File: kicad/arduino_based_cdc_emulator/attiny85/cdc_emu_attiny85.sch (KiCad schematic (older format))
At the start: 9 parts, among them IC1 ATTINY85-S, P1 CONN_5, U1 78L05

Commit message: board for attiny version vwcdavr smd
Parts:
- removed U1: 78L05, symbol 78L05
- added C3: 1u/6.3V, Capacitors_SMD:C_0805_HandSoldering, symbol CP
- added P2: CONN_01X03, Pin_Headers:Pin_Header_Straight_1x03, symbol CONN_01X03
- added U1: AP1117D50, TO_SOT_Packages_SMD:SOT-223, symbol AP1117D50
- added U2: LM78L05ACZ, Housings_SOT-23_SOT-143_TSOT-6:SOT-23, symbol LM78L05ACZ
- C1, C2: footprint (none) -> Capacitors_SMD:C_0805_HandSoldering; symbol C -> C-RESCUE-cdc_emu_attiny85
- IC1: symbol ATTINY85-S -> ATTINY85-S-RESCUE-cdc_emu_attiny85
- P1: value CONN_5 -> CONN_01X05; footprint (none) -> Pin_Headers:Pin_Header_Straight_1x05; symbol CONN_5 -> CONN_01X05
- R1, R2, R3, R4: footprint (none) -> Resistors_SMD:R_0805_HandSoldering; symbol R -> R-RESCUE-cdc_emu_attiny85
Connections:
- net labels added: MOSI, RST, TX
- wire segments 27 -> 41
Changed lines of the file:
@@
-EESchema Schematic File Version 2  date Tue 04 Mar 2014 02:18:31 PM CET
+EESchema Schematic File Version 2
+LIBS:cdc_emu_attiny85-rescue
 LIBS:power
 LIBS:device
@@
 LIBS:memory
 LIBS:xilinx
-LIBS:special
 LIBS:microcontrollers
 LIBS:dsp
@@
 LIBS:valves
 LIBS:cdc_emu_attiny85-cache
-EELAYER 25  0
+EELAYER 25 0
 EELAYER END
-$Descr A4 11700 8267
+$Descr A4 11693 8268
 encoding utf-8
 Sheet 1 1
@@
 	3950 3500 3500 3500
 Wire Wire Line
-	3950 3800 3850 3800
-Wire Wire Line
-	3850 3800 3850 3050
+	3500 3800 3950 3800
+Wire Wire Line
+	3850 3050 3850 3800
 Wire Wire Line
 	7400 3300 7300 3300
@@
 F 0 "#PWR01" H 8950 4350 20  0001 C CNN
 F 1 "+12V" H 8950 4500 30  0000 C CNN
+F 2 "" H 8950 4400 60  0001 C CNN
+F 3 "" H 8950 4400 60  0001 C CNN
 	1    8950 4400
 	1    0    0    -1
 $EndComp
 $Comp
-L GND #PWR02
+L GND-RESCUE-cdc_emu_attiny85 #PWR02
 U 1 1 531578E1
 P 9050 4550
 F 0 "#PWR02" H 9050 4550 30  0001 C CNN
 F 1 "GND" H 9050 4480 30  0001 C CNN
+F 2 "" H 9050 4550 60  0001 C CNN
+F 3 "" H 9050 4550 60  0001 C CNN
 	1    9050 4550
 	1    0    0    -1
@@
 DataIn
 $Comp
-L CONN_5 P1
+L CONN_01X05 P1
 U 1 1 531578B2
-P 9650 4250
-F 0 "P1" V 9600 4250 50  0000 C CNN
-F 1 "CONN_5" V 9700 4250 50  0000 C CNN
-	1    9650 4250
+P 9450 4250
+F 0 "P1" V 9400 4250 50  0000 C CNN
+F 1 "CONN_01X05" V 9500 4250 50  0000 C CNN
+F 2 "Pin_Headers:Pin_Header_Straight_1x05" H 9450 4250 60  0001 C CNN
+F 3 "" H 9450 4250 60  0001 C CNN
+	1    9450 4250
 	1    0    0    -1
 $EndComp
@@
 F 0 "#PWR03" H 6650 5350 20  0001 C CNN
 F 1 "+12V" H 6650 5500 30  0000 C CNN
+F 2 "" H 6650 5400 60  0001 C CNN
+F 3 "" H 6650 5400 60  0001 C CNN
 	1    6650 5400
 	1    0    0    -1
@@
 F 0 "#PWR04" H 7750 5490 20  0001 C CNN
 F 1 "+5V" H 7750 5490 30  0000 C CNN
+F 2 "" H 7750 5400 60  0001 C CNN
+F 3 "" H 7750 5400 60  0001 C CNN
 	1    7750 5400
 	1    0    0    -1
 $EndComp
 $Comp
-L GND #PWR05
+L GND-RESCUE-cdc_emu_attiny85 #PWR05
 U 1 1 53148A75
 P 7750 6100
 F 0 "#PWR05" H 7750 6100 30  0001 C CNN
 F 1 "GND" H 7750 6030 30  0001 C CNN
+F 2 "" H 7750 6100 60  0001 C CNN
+F 3 "" H 7750 6100 60  0001 C CNN
 	1    7750 6100
 	1    0    0    -1
 $EndComp
 $Comp
-L GND #PWR06
+L GND-RESCUE-cdc_emu_attiny85 #PWR06
 U 1 1 53148A72
 P 7200 6100
 F 0 "#PWR06" H 7200 6100 30  0001 C CNN
 F 1 "GND" H 7200 6030 30  0001 C CNN
+F 2 "" H 7200 6100 60  0001 C CNN
+F 3 "" H 7200 6100 60  0001 C CNN
 	1    7200 6100
 	1    0    0    -1
 $EndComp
 $Comp
-L GND #PWR07
+L GND-RESCUE-cdc_emu_attiny85 #PWR07
 U 1 1 53148A70
 P 6650 6100
 F 0 "#PWR07" H 6650 6100 30  0001 C CNN
 F 1 "GND" H 6650 6030 30  0001 C CNN
+F 2 "" H 6650 6100 60  0001 C CNN
+F 3 "" H 6650 6100 60  0001 C CNN
 	1    6650 6100
 	1    0    0    -1
 $EndComp
 $Comp
-L C C2
+L C-RESCUE-cdc_emu_attiny85 C2
 U 1 1 53148A27
 P 7750 5800
 F 0 "C2" H 7800 5900 50  0000 L CNN
 F 1 "100n" H 7800 5700 50  0000 L CNN
+F 2 "Capacitors_SMD:C_0805_HandSoldering" H 7750 5800 60  0001 C CNN
+F 3 "" H 7750 5800 60  0001 C CNN
 	1    7750 5800
 	1    0    0    -1
 $EndComp
 $Comp
-L C C1
+L C-RESCUE-cdc_emu_attiny85 C1
 U 1 1 53148A21
 P 6650 5800
 F 0 "C1" H 6700 5900 50  0000 L CNN
 F 1 "100n" H 6700 5700 50  0000 L CNN
+F 2 "Capacitors_SMD:C_0805_HandSoldering" H 6650 5800 60  0001 C CNN
+F 3 "" H 6650 5800 60  0001 C CNN
 	1    6650 5800
 	1    0    0    -1
 $EndComp
 $Comp
-L 78L05 U1
-U 1 1 53148A1A
-P 7200 5550
-F 0 "U1" H 7350 5354 60  0000 C CNN
-F 1 "78L05" H 7200 5750 60  0000 C CNN
-	1    7200 5550
-	1    0    0    -1
-$EndComp
-$Comp
-L GND #PWR08
+L GND-RESCUE-cdc_emu_attiny85 #PWR08
 U 1 1 53148A0A
 P 7300 3900
 F 0 "#PWR08" H 7300 3900 30  0001 C CNN
 F 1 "GND" H 7300 3830 30  0001 C CNN
+F 2 "" H 7300 3900 60  0001 C CNN
+F 3 "" H 7300 3900 60  0001 C CNN
 	1    7300 3900
 	1    0    0    -1
@@
 F 0 "#PWR09" H 7400 3040 20  0001 C CNN
 F 1 "+5V" H 7400 3040 30  0000 C CNN
+F 2 "" H 7400 2950 60  0001 C CNN
+F 3 "" H 7400 2950 60  0001 C CNN
 	1    7400 2950
 	1    0    0    -1
 $EndComp
 $Comp
-L R R3
+L R-RESCUE-cdc_emu_attiny85 R3
 U 1 1 531489A2
 P 4200 3700
-F 0 "R3" V 4280 3700 50  0000 C CNN
+F 0 "R3" V 4150 3900 50  0000 C CNN
 F 1 "3k3" V 4200 3700 50  0000 C CNN
+F 2 "Resistors_SMD:R_0805_HandSoldering" H 4200 3700 60  0001 C CNN
+F 3 "" H 4200 3700 60  0001 C CNN
 	1    4200 3700
 	0    -1   -1   0
 $EndComp
 $Comp
-L R R2
+L R-RESCUE-cdc_emu_attiny85 R2
 U 1 1 5314899E
 P 4200 3500
-F 0 "R2" V 4280 3500 50  0000 C CNN
+F 0 "R2" V 4150 3700 50  0000 C CNN
 F 1 "3k3" V 4200 3500 50  0000 C CNN
+F 2 "Resistors_SMD:R_0805_HandSoldering" H 4200 3500 60  0001 C CNN
+F 3 "" H 4200 3500 60  0001 C CNN
 	1    4200 3500
 	0    -1   -1   0
 $EndComp
 $Comp
-L R R1
+L R-RESCUE-cdc_emu_attiny85 R1
 U 1 1 53148999
 P 4200 3400
-F 0 "R1" V 4280 3400 50  0000 C CNN
+F 0 "R1" V 4150 3600 50  0000 C CNN
 F 1 "3k3" V 4200 3400 50  0000 C CNN
+F 2 "Resistors_SMD:R_0805_HandSoldering" H 4200 3400 60  0001 C CNN
+F 3 "" H 4200 3400 60  0001 C CNN
 	1    4200 3400
 	0    -1   -1   0
 $EndComp
 $Comp
-L R R4
+L R-RESCUE-cdc_emu_attiny85 R4
 U 1 1 53148995
 P 4200 3800
-F 0 "R4" V 4280 3800 50  0000 C CNN
+F 0 "R4" V 4100 4000 50  0000 C CNN
 F 1 "10k" V 4200 3800 50  0000 C CNN
+F 2 "Resistors_SMD:R_0805_HandSoldering" H 4200 3800 60  0001 C CNN
+F 3 "" H 4200 3800 60  0001 C CNN
 	1    4200 3800
 	0    -1   -1   0
 $EndComp
 $Comp
-L ATTINY85-S IC1
+L ATTINY85-S-RESCUE-cdc_emu_attiny85 IC1
 U 1 1 53148881
 P 4800 3200
@@
 F 1 "ATTINY85-S" H 6800 2450 60  0000 C CNN
 F 2 "DIP8" H 4900 2450 60  0001 C CNN
+F 3 "" H 4800 3200 60  0001 C CNN
 	1    4800 3200
 	1    0    0    -1
 $EndComp
+$Comp
+L CP C3
+U 1 1 560DAE88
+P 4550 4150
+F 0 "C3" H 4575 4250 50  0000 L CNN
+F 1 "1u/6.3V" H 4575 4050 50  0000 L CNN
+F 2 "Capacitors_SMD:C_0805_HandSoldering" H 4588 4000 30  0000 C CNN
+F 3 "" H 4550 4150 60  0000 C CNN
+	1    4550 4150
+	1    0    0    -1
+$EndComp
+Wire Wire Line
+	4550 4000 4550 3800
+Connection ~ 4550 3800
+Wire Wire Line
+	4550 4300 4550 4400
+$Comp
+L GND-RESCUE-cdc_emu_attiny85 #PWR010
+U 1 1 560DAF73
+P 4550 4400
+F 0 "#PWR010" H 4550 4400 30  0001 C CNN
+F 1 "GND" H 4550 4330 30  0001 C CNN
+F 2 "" H 4550 4400 60  0001 C CNN
+F 3 "" H 4550 4400 60  0001 C CNN
+	1    4550 4400
+	1    0    0    -1
+$EndComp
+Wire Wire Line
+	3500 3600 4600 3600
+Wire Wire Line
+	9250 3450 8450 3450
+Text Label 8450 3450 0    60   ~ 0
+TX
+Text Label 3500 3600 0    60   ~ 0
+TX
+Wire Wire Line
+	3500 3300 4600 3300
+Text Label 3500 3300 0    60   ~ 0
+MOSI
+Connection ~ 3850 3800
+Text Label 3500 3800 0    60   ~ 0
+RST
+Text Label 8450 3350 0    60   ~ 0
+MOSI
+Text Label 8450 3550 0    60   ~ 0
+RST
+Wire Wire Line
+	8450 3550 9250 3550
+Wire Wire Line
+	8450 3350 9250 3350
+$Comp
+L CONN_01X03 P2
+U 1 1 5628FA6F
+P 9450 3450
+F 0 "P2" V 9400 3450 50  0000 C CNN
+F 1 "CONN_01X03" V 9500 3450 50  0000 C CNN
+F 2 "Pin_Headers:Pin_Header_Straight_1x03" H 9450 3450 60  0001 C CNN
+F 3 "" H 9450 3450 60  0001 C CNN
+	1    9450 3450
+	1    0    0    -1
+$EndComp
+$Comp
+L AP1117D50 U1
+U 1 1 562904CD
+P 7200 4900
+F 0 "U1" H 7300 4650 50  0000 C CNN
+F 1 "AP1117D50" H 7200 5150 50  0000 C CNN
+F 2 "TO_SOT_Packages_SMD:SOT-223" H 7200 4900 60  0000 C CNN
+F 3 "" H 7200 4900 60  0000 C CNN
+	1    7200 4900
+	1    0    0    -1
+$EndComp
+Wire Wire Line
+	7200 5200 7450 5200
+Wire Wire Line
+	7450 5200 7450 5900
+Wire Wire Line
+	7450 5900 7200 5900
+Connection ~ 7200 5900
+Wire Wire Line
+	6750 4900 6900 4900
+Wire Wire Line
+	6750 4900 6750 5500
+Connection ~ 6750 5500
+Wire Wire Line
+	7650 5500 7650 4900
+Wire Wire Line
+	7650 4900 7500 4900
+Connection ~ 7650 5500
+$Comp
+L LM78L05ACZ U2
+U 1 1 56290767
+P 7200 5550
+F 0 "U2" H 7000 5750 40  0000 C CNN
+F 1 "LM78L05ACZ" H 7200 5750 40  0000 L CNN
+F 2 "Housings_SOT-23_SOT-143_TSOT-6:SOT-23" H 7200 5650 30  0000 C CIN
+F 3 "" H 7200 5550 60  0000 C CNN
+	1    7200 5550
+	1    0    0    -1
+$EndComp

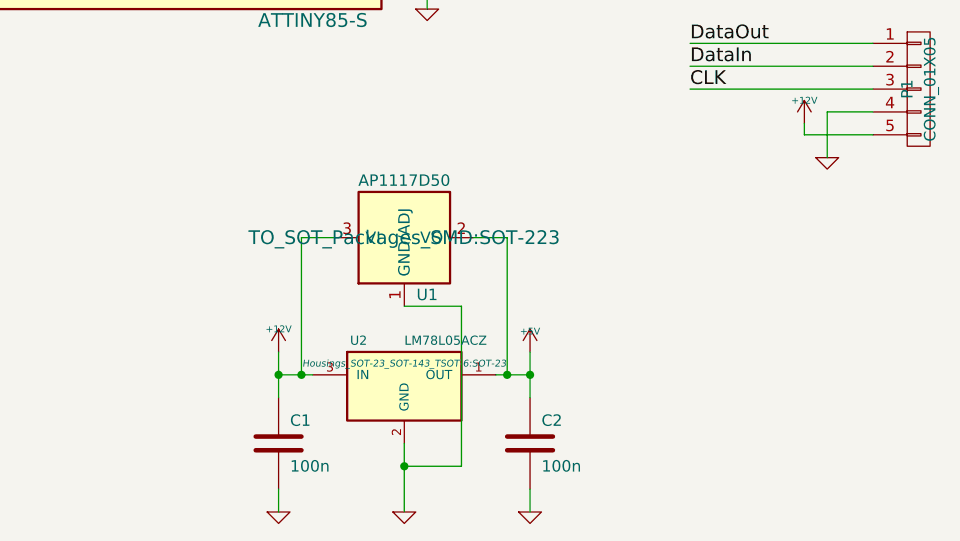
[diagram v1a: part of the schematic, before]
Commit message: fix 78L05 pinout, 5V connection from U1
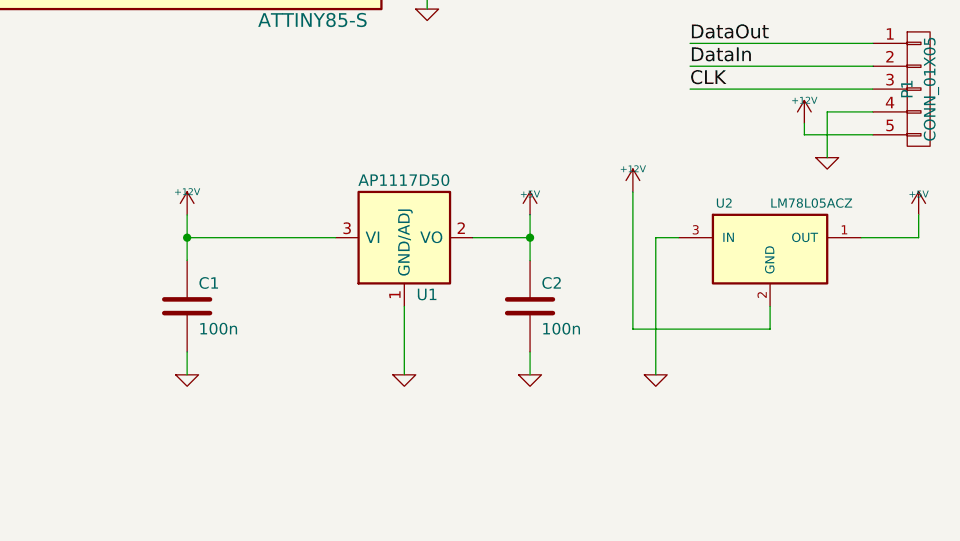
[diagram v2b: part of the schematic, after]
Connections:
- net +12V: now also U2.2 (GND); no longer U2.3 (IN)
- net GND: now also U2.3 (IN); no longer U2.2 (GND)
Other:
- moved on the sheet: C1, C2, U2
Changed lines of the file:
@@
 Comment4 ""
 $EndDescr
-Wire Wire Line
-	8950 4400 8950 4450
-Wire Wire Line
-	8950 4450 9250 4450
-Wire Wire Line
-	4450 3500 4600 3500
-Wire Wire Line
-	4450 3800 4600 3800
-Wire Wire Line
-	7400 3050 3850 3050
-Wire Wire Line
-	9250 4250 8450 4250
-Wire Wire Line
-	9250 4050 8450 4050
-Wire Wire Line
-	7750 6000 7750 6100
-Wire Wire Line
-	6650 6000 6650 6100
-Wire Wire Line
-	6650 5500 6800 5500
-Wire Wire Line
-	7750 5400 7750 5600
-Connection ~ 7400 3050
-Wire Wire Line
-	7400 2950 7400 3300
-Wire Wire Line
-	3950 3700 3500 3700
-Wire Wire Line
-	3500 3400 3950 3400
-Wire Wire Line
-	3950 3500 3500 3500
-Wire Wire Line
-	3500 3800 3950 3800
-Wire Wire Line
-	3850 3050 3850 3800
-Wire Wire Line
-	7400 3300 7300 3300
-Wire Wire Line
-	7600 5500 7750 5500
-Connection ~ 7750 5500
-Wire Wire Line
-	6650 5400 6650 5600
-Connection ~ 6650 5500
-Wire Wire Line
-	7200 5800 7200 6100
-Wire Wire Line
-	9250 4150 8450 4150
-Wire Wire Line
-	4450 3400 4600 3400
-Wire Wire Line
-	4450 3700 4600 3700
-Wire Wire Line
-	7300 3800 7300 3900
-Wire Wire Line
-	9250 4350 9050 4350
-Wire Wire Line
-	9050 4350 9050 4550
 $Comp
 L +12V #PWR01
@@
 L +12V #PWR03
 U 1 1 53148C3B
-P 6650 5400
-F 0 "#PWR03" H 6650 5350 20  0001 C CNN
-F 1 "+12V" H 6650 5500 30  0000 C CNN
-F 2 "" H 6650 5400 60  0001 C CNN
-F 3 "" H 6650 5400 60  0001 C CNN
-	1    6650 5400
+P 6250 4800
+F 0 "#PWR03" H 6250 4750 20  0001 C CNN
+F 1 "+12V" H 6250 4900 30  0000 C CNN
+F 2 "" H 6250 4800 60  0001 C CNN
+F 3 "" H 6250 4800 60  0001 C CNN
+	1    6250 4800
 	1    0    0    -1
 $EndComp
@@
 L +5V #PWR04
 U 1 1 53148C2D
-P 7750 5400
-F 0 "#PWR04" H 7750 5490 20  0001 C CNN
-F 1 "+5V" H 7750 5490 30  0000 C CNN
-F 2 "" H 7750 5400 60  0001 C CNN
-F 3 "" H 7750 5400 60  0001 C CNN
-	1    7750 5400
+P 7750 4800
+F 0 "#PWR04" H 7750 4890 20  0001 C CNN
+F 1 "+5V" H 7750 4890 30  0000 C CNN
+F 2 "" H 7750 4800 60  0001 C CNN
+F 3 "" H 7750 4800 60  0001 C CNN
+	1    7750 4800
 	1    0    0    -1
 $EndComp
@@
 L GND-RESCUE-cdc_emu_attiny85 #PWR05
 U 1 1 53148A75
-P 7750 6100
-F 0 "#PWR05" H 7750 6100 30  0001 C CNN
-F 1 "GND" H 7750 6030 30  0001 C CNN
-F 2 "" H 7750 6100 60  0001 C CNN
-F 3 "" H 7750 6100 60  0001 C CNN
-	1    7750 6100
+P 7750 5500
+F 0 "#PWR05" H 7750 5500 30  0001 C CNN
+F 1 "GND" H 7750 5430 30  0001 C CNN
+F 2 "" H 7750 5500 60  0001 C CNN
+F 3 "" H 7750 5500 60  0001 C CNN
+	1    7750 5500
 	1    0    0    -1
 $EndComp
@@
 L GND-RESCUE-cdc_emu_attiny85 #PWR06
 U 1 1 53148A72
-P 7200 6100
-F 0 "#PWR06" H 7200 6100 30  0001 C CNN
-F 1 "GND" H 7200 6030 30  0001 C CNN
-F 2 "" H 7200 6100 60  0001 C CNN
-F 3 "" H 7200 6100 60  0001 C CNN
-	1    7200 6100
+P 7200 5500
+F 0 "#PWR06" H 7200 5500 30  0001 C CNN
+F 1 "GND" H 7200 5430 30  0001 C CNN
+F 2 "" H 7200 5500 60  0001 C CNN
+F 3 "" H 7200 5500 60  0001 C CNN
+	1    7200 5500
 	1    0    0    -1
 $EndComp
@@
 L GND-RESCUE-cdc_emu_attiny85 #PWR07
 U 1 1 53148A70
-P 6650 6100
-F 0 "#PWR07" H 6650 6100 30  0001 C CNN
-F 1 "GND" H 6650 6030 30  0001 C CNN
-F 2 "" H 6650 6100 60  0001 C CNN
-F 3 "" H 6650 6100 60  0001 C CNN
-	1    6650 6100
+P 6250 5500
+F 0 "#PWR07" H 6250 5500 30  0001 C CNN
+F 1 "GND" H 6250 5430 30  0001 C CNN
+F 2 "" H 6250 5500 60  0001 C CNN
+F 3 "" H 6250 5500 60  0001 C CNN
+	1    6250 5500
 	1    0    0    -1
 $EndComp
@@
 L C-RESCUE-cdc_emu_attiny85 C2
 U 1 1 53148A27
-P 7750 5800
-F 0 "C2" H 7800 5900 50  0000 L CNN
-F 1 "100n" H 7800 5700 50  0000 L CNN
-F 2 "Capacitors_SMD:C_0805_HandSoldering" H 7750 5800 60  0001 C CNN
-F 3 "" H 7750 5800 60  0001 C CNN
-	1    7750 5800
+P 7750 5200
+F 0 "C2" H 7800 5300 50  0000 L CNN
+F 1 "100n" H 7800 5100 50  0000 L CNN
+F 2 "Capacitors_SMD:C_0805_HandSoldering" H 7750 5200 60  0001 C CNN
+F 3 "" H 7750 5200 60  0001 C CNN
+	1    7750 5200
 	1    0    0    -1
 $EndComp
@@
 L C-RESCUE-cdc_emu_attiny85 C1
 U 1 1 53148A21
-P 6650 5800
-F 0 "C1" H 6700 5900 50  0000 L CNN
-F 1 "100n" H 6700 5700 50  0000 L CNN
-F 2 "Capacitors_SMD:C_0805_HandSoldering" H 6650 5800 60  0001 C CNN
-F 3 "" H 6650 5800 60  0001 C CNN
-	1    6650 5800
+P 6250 5200
+F 0 "C1" H 6300 5300 50  0000 L CNN
+F 1 "100n" H 6300 5100 50  0000 L CNN
+F 2 "Capacitors_SMD:C_0805_HandSoldering" H 6250 5200 60  0001 C CNN
+F 3 "" H 6250 5200 60  0001 C CNN
+	1    6250 5200
 	1    0    0    -1
 $EndComp
@@
 	1    0    0    -1
 $EndComp
-Wire Wire Line
-	4550 4000 4550 3800
-Connection ~ 4550 3800
-Wire Wire Line
-	4550 4300 4550 4400
 $Comp
 L GND-RESCUE-cdc_emu_attiny85 #PWR010
@@
 	1    0    0    -1
 $EndComp
-Wire Wire Line
-	3500 3600 4600 3600
-Wire Wire Line
-	9250 3450 8450 3450
 Text Label 8450 3450 0    60   ~ 0
 TX
 Text Label 3500 3600 0    60   ~ 0
 TX
-Wire Wire Line
-	3500 3300 4600 3300
 Text Label 3500 3300 0    60   ~ 0
 MOSI
-Connection ~ 3850 3800
 Text Label 3500 3800 0    60   ~ 0
 RST
@@
 Text Label 8450 3550 0    60   ~ 0
 RST
-Wire Wire Line
-	8450 3550 9250 3550
-Wire Wire Line
-	8450 3350 9250 3350
 $Comp
 L CONN_01X03 P2
@@
 F 0 "U1" H 7300 4650 50  0000 C CNN
 F 1 "AP1117D50" H 7200 5150 50  0000 C CNN
-F 2 "TO_SOT_Packages_SMD:SOT-223" H 7200 4900 60  0000 C CNN
+F 2 "TO_SOT_Packages_SMD:SOT-223" H 7200 4900 60  0001 C CNN
 F 3 "" H 7200 4900 60  0000 C CNN
 	1    7200 4900
 	1    0    0    -1
 $EndComp
-Wire Wire Line
-	7200 5200 7450 5200
-Wire Wire Line
-	7450 5200 7450 5900
-Wire Wire Line
-	7450 5900 7200 5900
-Connection ~ 7200 5900
-Wire Wire Line
-	6750 4900 6900 4900
-Wire Wire Line
-	6750 4900 6750 5500
-Connection ~ 6750 5500
-Wire Wire Line
-	7650 5500 7650 4900
-Wire Wire Line
-	7650 4900 7500 4900
-Connection ~ 7650 5500
 $Comp
 L LM78L05ACZ U2
 U 1 1 56290767
-P 7200 5550
-F 0 "U2" H 7000 5750 40  0000 C CNN
-F 1 "LM78L05ACZ" H 7200 5750 40  0000 L CNN
-F 2 "Housings_SOT-23_SOT-143_TSOT-6:SOT-23" H 7200 5650 30  0000 C CIN
-F 3 "" H 7200 5550 60  0000 C CNN
-	1    7200 5550
-	1    0    0    -1
-$EndComp
+P 8800 4950
+F 0 "U2" H 8600 5150 40  0000 C CNN
+F 1 "LM78L05ACZ" H 8800 5150 40  0000 L CNN
+F 2 "Housings_SOT-23_SOT-143_TSOT-6:SOT-23" H 8800 5050 30  0001 C CIN
+F 3 "" H 8800 4950 60  0000 C CNN
+	1    8800 4950
+	1    0    0    -1
+$EndComp
+Wire Wire Line
+	8950 4400 8950 4450
+Wire Wire Line
+	8950 4450 9250 4450
+Wire Wire Line
+	4450 3500 4600 3500
+Wire Wire Line
+	4450 3800 4600 3800
+Wire Wire Line
+	7400 3050 3850 3050
+Wire Wire Line
+	9250 4250 8450 4250
+Wire Wire Line
+	9250 4050 8450 4050
+Wire Wire Line
+	7750 5400 7750 5500
+Wire Wire Line
+	6250 5400 6250 5500
+Wire Wire Line
+	6250 4900 6900 4900
+Connection ~ 7400 3050
+Wire Wire Line
+	7400 2950 7400 3300
+Wire Wire Line
+	3950 3700 3500 3700
+Wire Wire Line
+	3500 3400 3950 3400
+Wire Wire Line
+	3950 3500 3500 3500
+Wire Wire Line
+	3500 3800 3950 3800
+Wire Wire Line
+	3850 3050 3850 3800
+Wire Wire Line
+	7400 3300 7300 3300
+Wire Wire Line
+	6250 4800 6250 5000
+Connection ~ 6250 4900
+Wire Wire Line
+	9250 4150 8450 4150
+Wire Wire Line
+	4450 3400 4600 3400
+Wire Wire Line
+	4450 3700 4600 3700
+Wire Wire Line
+	7300 3800 7300 3900
+Wire Wire Line
+	9250 4350 9050 4350
+Wire Wire Line
+	9050 4350 9050 4550
+Wire Wire Line
+	4550 4000 4550 3800
+Connection ~ 4550 3800
+Wire Wire Line
+	4550 4300 4550 4400
+Wire Wire Line
+	3500 3600 4600 3600
+Wire Wire Line
+	9250 3450 8450 3450
+Wire Wire Line
+	3500 3300 4600 3300
+Connection ~ 3850 3800
+Wire Wire Line
+	8450 3550 9250 3550
+Wire Wire Line
+	8450 3350 9250 3350
+Wire Wire Line
+	7500 4900 7750 4900
+Wire Wire Line
+	7200 5500 7200 5200
+Wire Wire Line
+	7750 4800 7750 5000
+Connection ~ 7750 4900
+$Comp
+L GND-RESCUE-cdc_emu_attiny85 #PWR?
+U 1 1 56E18351
+P 8300 5500
+F 0 "#PWR?" H 8300 5500 30  0001 C CNN
+F 1 "GND" H 8300 5430 30  0001 C CNN
+F 2 "" H 8300 5500 60  0001 C CNN
+F 3 "" H 8300 5500 60  0001 C CNN
+	1    8300 5500
+	1    0    0    -1
+$EndComp
+Wire Wire Line
+	8300 4900 8300 5500
+$Comp
+L +5V #PWR?
+U 1 1 56E18370
+P 9450 4800
+F 0 "#PWR?" H 9450 4890 20  0001 C CNN
+F 1 "+5V" H 9450 4890 30  0000 C CNN
+F 2 "" H 9450 4800 60  0001 C CNN
+F 3 "" H 9450 4800 60  0001 C CNN
+	1    9450 4800
+	1    0    0    -1
+$EndComp
+Wire Wire Line
+	9200 4900 9450 4900
+Wire Wire Line
+	9450 4900 9450 4800
+$Comp
+L +12V #PWR?
+U 1 1 56E184F4
+P 8200 4700
+F 0 "#PWR?" H 8200 4650 20  0001 C CNN
+F 1 "+12V" H 8200 4800 30  0000 C CNN
+F 2 "" H 8200 4700 60  0001 C CNN
+F 3 "" H 8200 4700 60  0001 C CNN
+	1    8200 4700
+	1    0    0    -1
+$EndComp
+Wire Wire Line
+	8200 4700 8200 5300
+Wire Wire Line
+	8300 4900 8400 4900
+Wire Wire Line
+	8200 5300 8800 5300
+Wire Wire Line
+	8800 5300 8800 5200
 $EndSCHEMATC

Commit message: right package for attiny85
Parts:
- IC1: footprint DIP8 -> my_modules:SOIC-8-N_wide_pads
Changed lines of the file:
@@
 F 0 "IC1" H 4900 3250 60  0000 C CNN
 F 1 "ATTINY85-S" H 6800 2450 60  0000 C CNN
-F 2 "DIP8" H 4900 2450 60  0001 C CNN
+F 2 "my_modules:SOIC-8-N_wide_pads" H 4900 2450 60  0001 C CNN
 F 3 "" H 4800 3200 60  0001 C CNN
 	1    4800 3200
